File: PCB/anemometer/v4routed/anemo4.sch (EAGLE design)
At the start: 64 parts, among them IC1 AD8223, IC2 AD8223, IC3 AD8223, IC4 AD8223, IC6 TL072D, J1 RJ12STRAIGHT-I2C, J2 RJ12STRAIGHT-I2C, T1 BC846, T2 BC846, T3 BC846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

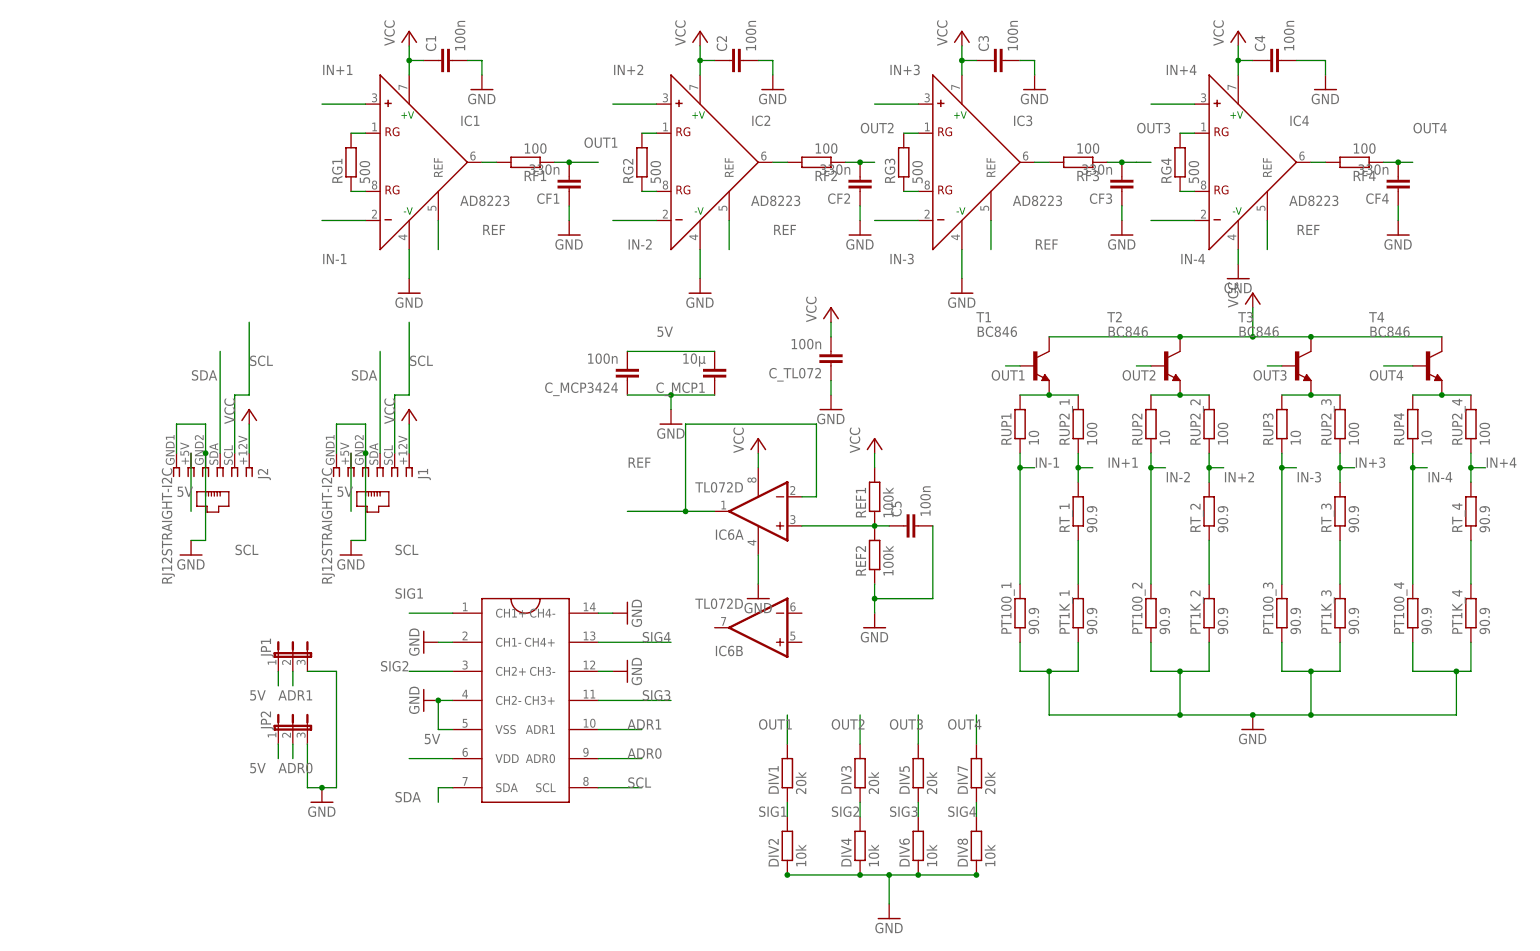
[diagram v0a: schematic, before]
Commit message: routed anemometer and integrated bertha with ground planes and separate analog and digital ground. ready for fabrication
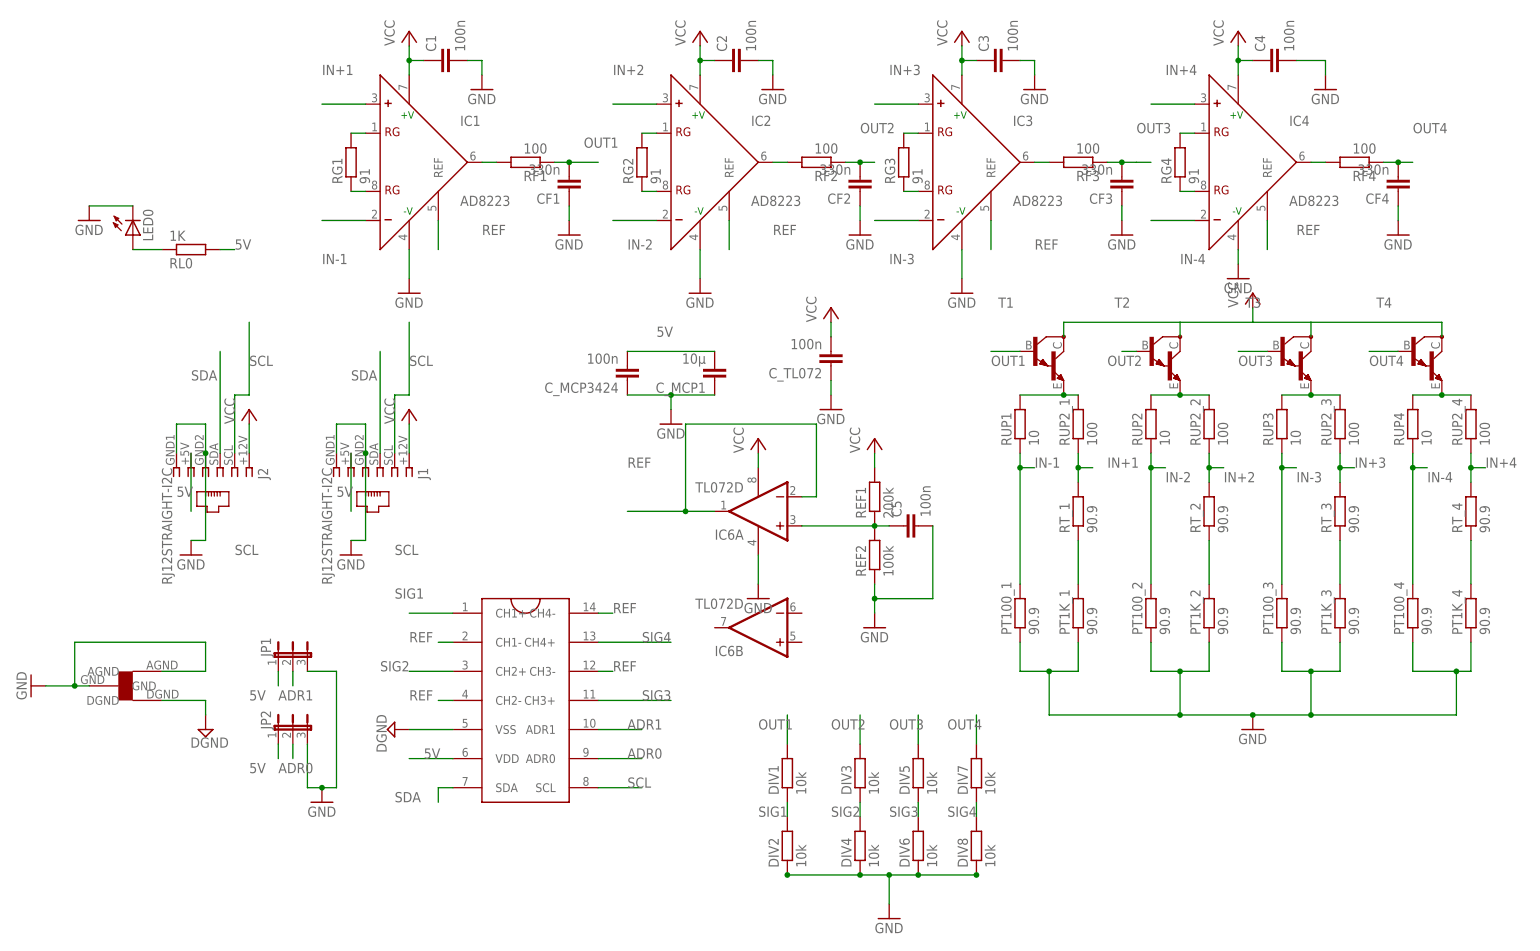
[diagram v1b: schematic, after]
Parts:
- added LED0: (no value), SparkFun:LED1206
- added RL0: 1K, resistor:R-EU_M1206
- added U$2: STARGND, lpatiny:STARGND
- DIV1, DIV3, DIV5, DIV7: value 20k -> 10k
- REF1: value 100k -> 200k
- RG1, RG2, RG3, RG4: value 500 -> 91
- T1, T2, T3, T4: value BC846 -> (none); device transistor:BC846 -> transistor:MMBTA13LT1-NPN_DARL-SOT23-BEC
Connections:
- new net DGND: U$1.VSS, U$2.DGND
- new net N$14: LED0.A, RL0.1
- net 5V: now also RL0.2
- net GND: now also LED0.C, U$2.AGND, U$2.GND; no longer U$1.CH1-, U$1.CH2-, U$1.CH3-, U$1.CH4-, U$1.VSS
- net REF: now also U$1.CH1-, U$1.CH2-, U$1.CH3-, U$1.CH4-

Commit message: integratedBertha v1.1: adjusted labels to good position. Anemometer: added ferrite bead for vcc decoupling and ground line.
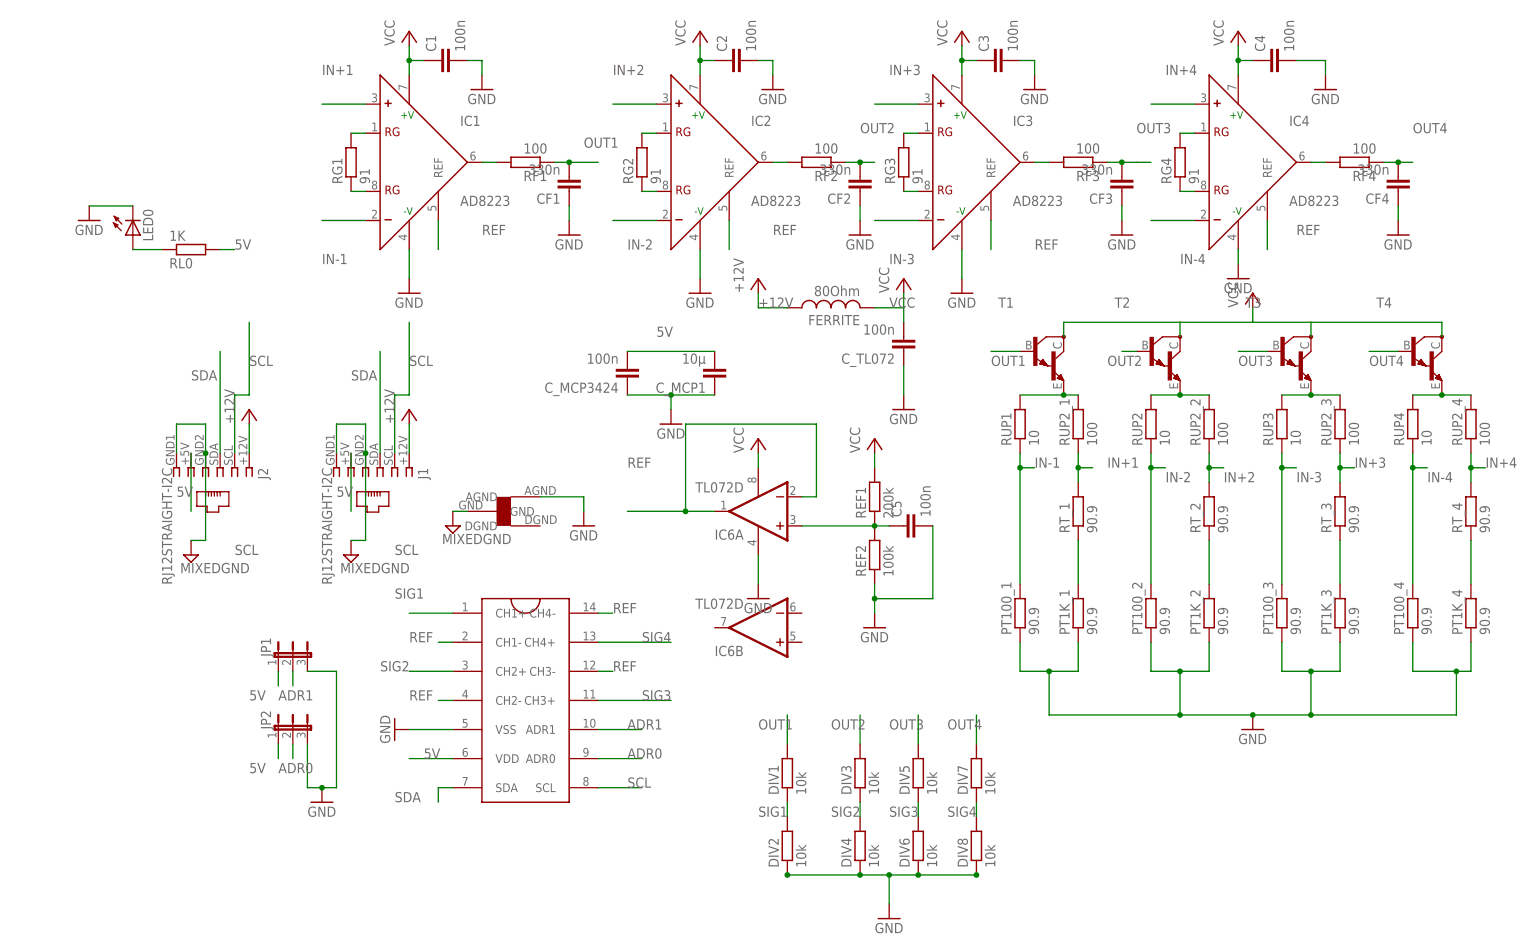
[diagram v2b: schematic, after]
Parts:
- added FERRITE: 80Ohm, rcl:L-USL3216C
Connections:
- removed net DGND: U$1.VSS, U$2.DGND
- new net +12V: FERRITE.1, J1.1, J2.1
- new net MIXEDGND: J1.4, J1.6, J2.4, J2.6, U$2.GND
- net GND: now also U$1.VSS; no longer J1.4, J1.6, J2.4, J2.6, U$2.GND
- net VCC: now also FERRITE.2; no longer J1.1, J2.1
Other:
- moved on the sheet: C_TL072

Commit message: added relay card with jumpers. adjusted labels in anemometer
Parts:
- FERRITE: value 80Ohm -> 80R Ferrite
- PT1K_1, PT1K_2, PT1K_3, PT1K_4: value 90.9 -> 909
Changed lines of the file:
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@@
 <part name="U$1" library="mcp3424" deviceset="MCP3424(SO14)" device=""/>
 <part name="GND23" library="supply1" deviceset="GND" device=""/>
-<part name="PT1K_1" library="resistor" deviceset="R-EU_" device="M1206" value="90.9"/>
+<part name="PT1K_1" library="resistor" deviceset="R-EU_" device="M1206" value="909"/>
 <part name="PT100_1" library="resistor" deviceset="R-EU_" device="M1206" value="90.9"/>
 <part name="PT100_2" library="resistor" deviceset="R-EU_" device="M1206" value="90.9"/>
 <part name="PT100_3" library="resistor" deviceset="R-EU_" device="M1206" value="90.9"/>
 <part name="PT100_4" library="resistor" deviceset="R-EU_" device="M1206" value="90.9"/>
-<part name="PT1K_2" library="resistor" deviceset="R-EU_" device="M1206" value="90.9"/>
-<part name="PT1K_3" library="resistor" deviceset="R-EU_" device="M1206" value="90.9"/>
-<part name="PT1K_4" library="resistor" deviceset="R-EU_" device="M1206" value="90.9"/>
+<part name="PT1K_2" library="resistor" deviceset="R-EU_" device="M1206" value="909"/>
+<part name="PT1K_3" library="resistor" deviceset="R-EU_" device="M1206" value="909"/>
+<part name="PT1K_4" library="resistor" deviceset="R-EU_" device="M1206" value="909"/>
 <part name="IC1" library="analog-devices" deviceset="AD620" device="R" value="AD8223"/>
 <part name="IC2" library="analog-devices" deviceset="AD620" device="R" value="AD8223"/>
@@
 <part name="LED0" library="SparkFun" deviceset="LED" device="1206"/>
 <part name="GND26" library="supply1" deviceset="GND" device=""/>
-<part name="FERRITE" library="rcl" deviceset="L-US" device="L3216C" value="80Ohm"/>
+<part name="FERRITE" library="rcl" deviceset="L-US" device="L3216C" value="80R Ferrite"/>
 <part name="P+11" library="supply1" deviceset="VCC" device="" value="+12V"/>
 <part name="GND19" library="supply1" deviceset="GND" device=""/>
